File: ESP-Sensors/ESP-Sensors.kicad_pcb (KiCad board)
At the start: 2 copper layers, 58.4 x 54 mm, 24 parts, among them J1 PROG_CONN, J2 GPIO, J3 SPI, J4 +3.3V GND +5V, J5 DEEP_SLEEP, SW1 RESET, SW2 PROG, U1 ESP-12E, U2 HT7333

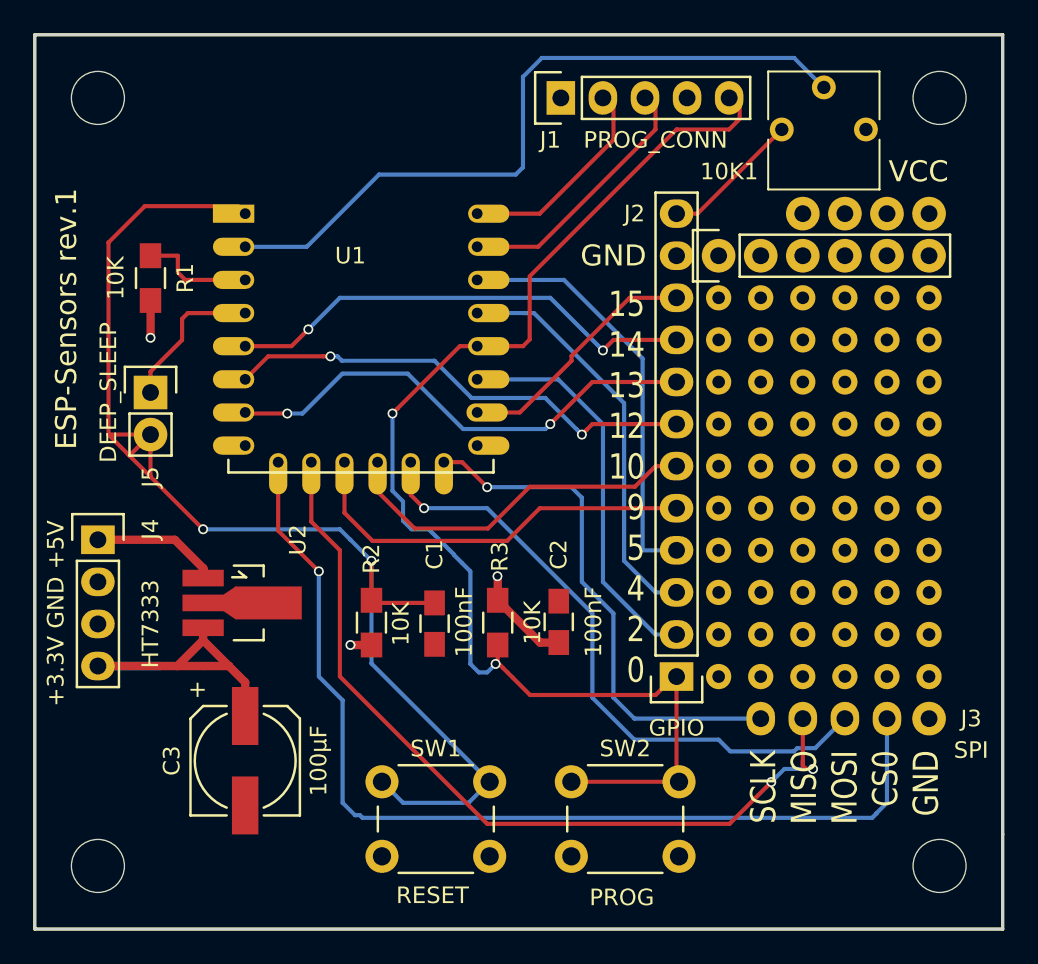
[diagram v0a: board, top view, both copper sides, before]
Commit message: Fixed ESP-Sensors board (ht7333 wrong footprint):rev 2
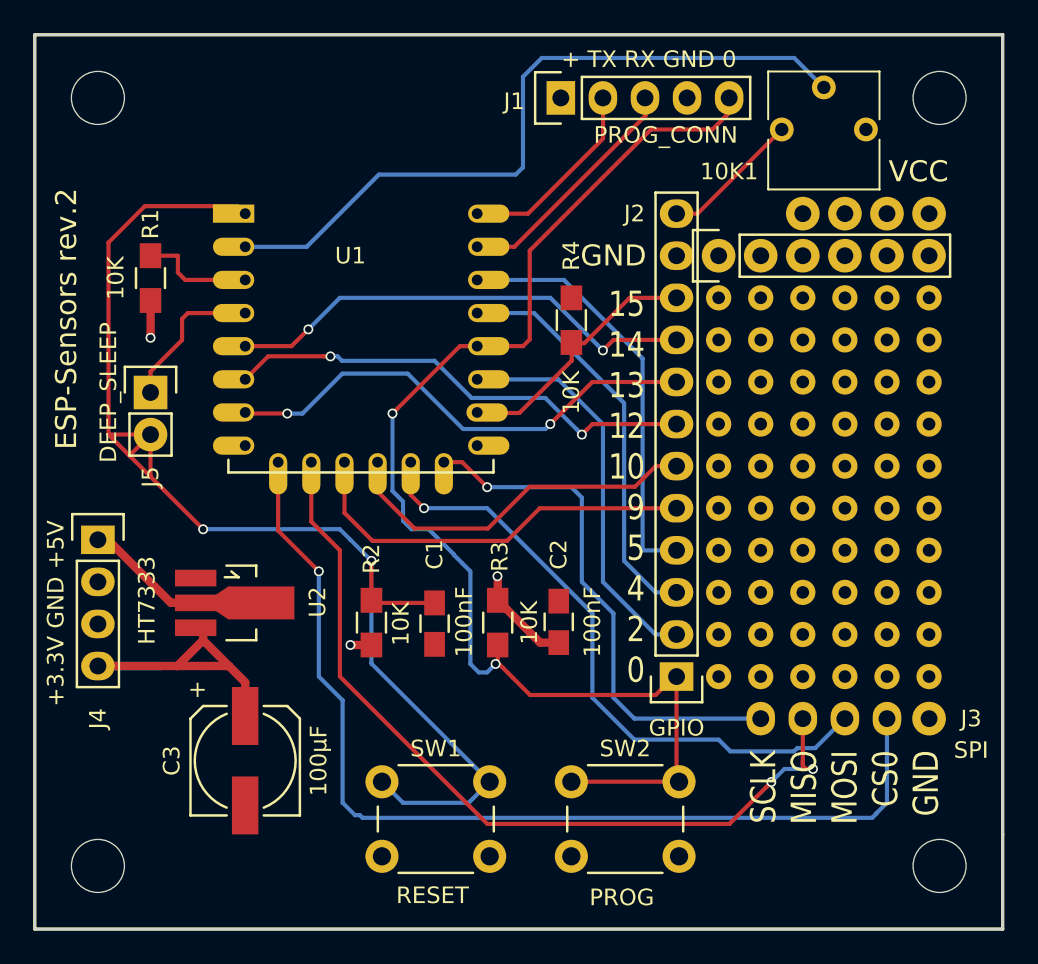
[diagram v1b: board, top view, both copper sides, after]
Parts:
- added R4: 10K, Resistors_SMD:R_0805_HandSoldering, F.Cu at (139.7, 78.8)
- J1: footprint Pin_Headers:Pin_Header_Straight_1x05 -> ESP-RS232:Pin_Header_Straight_1x05b
- moved J1 6.28 mm to (144.4, 62.1), turned to 0 degrees
- moved U2 0.45 mm to (119.4, 95.9)
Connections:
- U2 pad 1: Net-(J4-Pad1) -> GND
- U2 pad 2: GND -> Net-(J4-Pad1)
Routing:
- net Net-(J4-Pad1): track 7.84 -> 10.8 mm
- net /RXD: track 15.6 -> 14.4 mm
- net /TXD: track 12.6 -> 11.9 mm
- net /GPIO15: track 15.1 -> 15.6 mm
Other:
- board text added: "ESP-Sensors rev.2"
- board text removed: "ESP-Sensors rev.1"
